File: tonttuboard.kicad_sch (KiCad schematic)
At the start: 45 parts, among them U3 ICM-40609-D, U4 BMP388, U5 W25Q256JVFIQT, U6 MMC5983MA, U9 Teensy 4.0

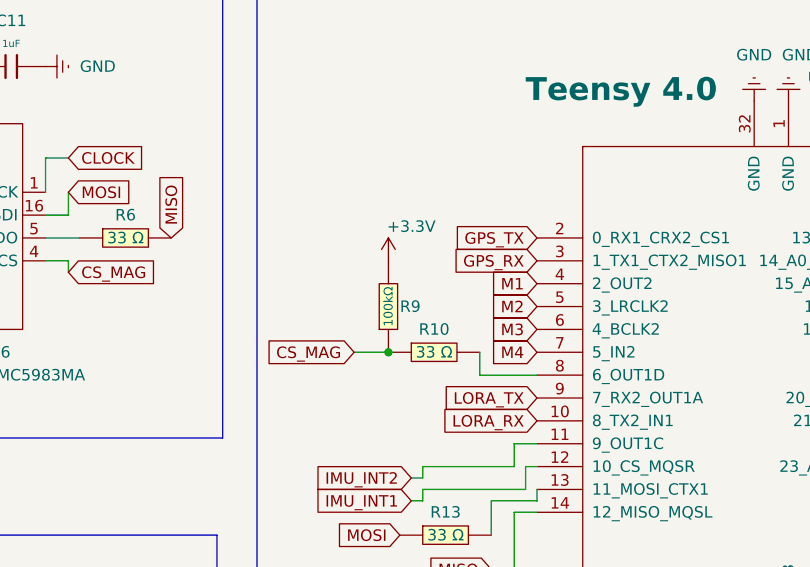
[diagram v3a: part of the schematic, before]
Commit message: Changed the CS Magnetometer 100 kohm pull-up to 4.7 kohm pulldown
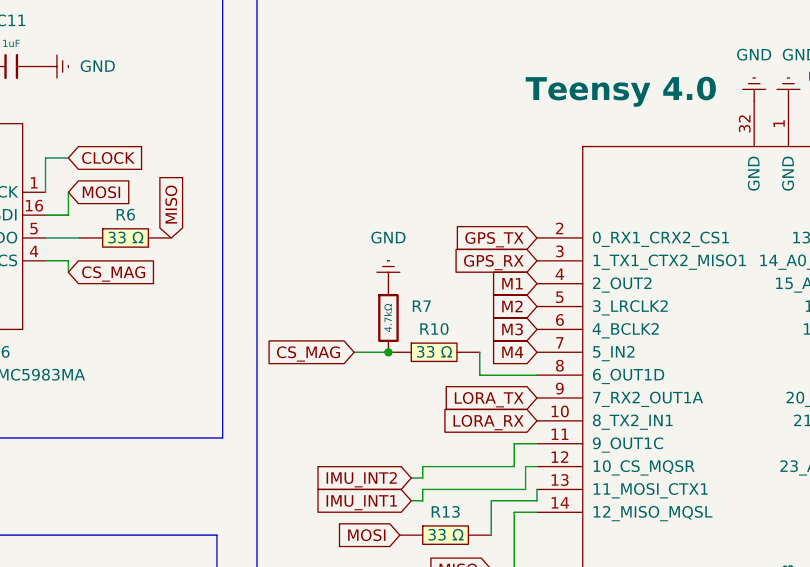
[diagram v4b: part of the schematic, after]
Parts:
- removed R9: 0603WAF1003T5E, EasyEDA:R0603, symbol EasyEDA:0603WAF1003T5E
- added R7: 4.7kΩ, PCM_JLCPCB:R_0603, symbol PCM_JLCPCB-Resistors:0603,4.7kΩ
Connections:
- net CS_MAG: now also R7.2
- net GND: now also R7.1
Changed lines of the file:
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@@
 	)
 	(junction
+		(at 179.07 66.04)
+		(diameter 0)
+		(color 0 0 0 0)
+	)
+	(junction
 		(at 58.42 97.79)
 		(diameter 0)
@@
 	)
 	(junction
-		(at 179.07 66.04)
-		(diameter 0)
-		(color 0 0 0 0)
-	)
-	(junction
 		(at 127 95.25)
 		(diameter 0)
@@
 	)
 	(symbol
-		(lib_id "power:+3.3V")
-		(at 179.07 55.88 0)
-		(unit 1)
-		(exclude_from_sim no)
-		(in_bom yes)
-		(on_board yes)
-		(dnp no)
-		(property "Reference" "#PWR042"
-			(at 179.07 59.69 0)
-			(effects
-				(font
-					(size 1.27 1.27)
-				)
-				(hide yes)
-			)
-		)
-		(property "Value" "+3.3V"
-			(at 181.61 52.07 0)
-			(effects
-				(font
-					(size 1.27 1.27)
-				)
-			)
-		)
-		(property "Footprint" ""
-			(at 179.07 55.88 0)
-			(effects
-				(font
-					(size 1.27 1.27)
-				)
-				(hide yes)
-			)
-		)
-		(property "Datasheet" ""
-			(at 179.07 55.88 0)
-			(effects
-				(font
-					(size 1.27 1.27)
-				)
-				(hide yes)
-			)
-		)
-		(property "Description" "Power symbol creates a global label with name \"+3.3V\""
-			(at 179.07 55.88 0)
-			(effects
-				(font
-					(size 1.27 1.27)
-				)
-				(hide yes)
-			)
-		)
-		(pin "1"
-		)
-		(instances
-			(project "tonttulauta v.0"
-				(path "/b9cca3cd-cb2d-42d4-a628-737eddf4a5c6"
-					(reference "#PWR042")
-					(unit 1)
-				)
-			)
-		)
-	)
-	(symbol
 		(lib_id "EasyEDA:BMP388")
 		(at 64.77 45.72 0)
@@
 	)
 	(symbol
+		(lib_id "PCM_JLCPCB-Resistors:0603,4.7kΩ")
+		(at 179.07 62.23 0)
+		(unit 1)
+		(exclude_from_sim no)
+		(in_bom yes)
+		(on_board yes)
+		(dnp no)
+		(property "Reference" "R7"
+			(at 181.61 60.96 0)
+			(effects
+				(font
+					(size 1.27 1.27)
+				)
+				(justify left)
+			)
+		)
+		(property "Value" "4.7kΩ"
+			(at 179.07 62.23 90)
+			(do_not_autoplace yes)
+			(effects
+				(font
+					(size 0.8 0.8)
+				)
+			)
+		)
+		(property "Footprint" "PCM_JLCPCB:R_0603"
+			(at 177.292 62.23 90)
+			(effects
+				(font
+					(size 1.27 1.27)
+				)
+				(hide yes)
+			)
+		)
+		(property "Datasheet" "https://www.lcsc.com/datasheet/lcsc_datasheet_2206010116_UNI-ROYAL-Uniroyal-Elec-0603WAF4701T5E_C23162.pdf"
+			(at 179.07 62.23 0)
+			(effects
+				(font
+					(size 1.27 1.27)
+				)
+				(hide yes)
+			)
+		)
+		(property "Description" "100mW Thick Film Resistors 75V ±100ppm/°C ±1% 4.7kΩ 0603 Chip Resistor - Surface Mount ROHS"
+			(at 179.07 62.23 0)
+			(effects
+				(font
+					(size 1.27 1.27)
+				)
+				(hide yes)
+			)
+		)
+		(property "LCSC" "C23162"
+			(at 179.07 62.23 0)
+			(effects
+				(font
+					(size 1.27 1.27)
+				)
+				(hide yes)
+			)
+		)
+		(property "Stock" "11302490"
+			(at 179.07 62.23 0)
+			(effects
+				(font
+					(size 1.27 1.27)
+				)
+				(hide yes)
+			)
+		)
+		(property "Price" "0.004USD"
+			(at 179.07 62.23 0)
+			(effects
+				(font
+					(size 1.27 1.27)
+				)
+				(hide yes)
+			)
+		)
+		(property "Process" "SMT"
+			(at 179.07 62.23 0)
+			(effects
+				(font
+					(size 1.27 1.27)
+				)
+				(hide yes)
+			)
+		)
+		(property "Minimum Qty" "20"
+			(at 179.07 62.23 0)
+			(effects
+				(font
+					(size 1.27 1.27)
+				)
+				(hide yes)
+			)
+		)
+		(property "Attrition Qty" "10"
+			(at 179.07 62.23 0)
+			(effects
+				(font
+					(size 1.27 1.27)
+				)
+				(hide yes)
+			)
+		)
+		(property "Class" "Basic Component"
+			(at 179.07 62.23 0)
+			(effects
+				(font
+					(size 1.27 1.27)
+				)
+				(hide yes)
+			)
+		)
+		(property "Category" "Resistors,Chip Resistor - Surface Mount"
+			(at 179.07 62.23 0)
+			(effects
+				(font
+					(size 1.27 1.27)
+				)
+				(hide yes)
+			)
+		)
+		(property "Manufacturer" "UNI-ROYAL(Uniroyal Elec)"
+			(at 179.07 62.23 0)
+			(effects
+				(font
+					(size 1.27 1.27)
+				)
+				(hide yes)
+			)
+		)
+		(property "Part" "0603WAF4701T5E"
+			(at 179.07 62.23 0)
+			(effects
+				(font
+					(size 1.27 1.27)
+				)
+				(hide yes)
+			)
+		)
+		(property "Resistance" "4.7kΩ"
+			(at 179.07 62.23 0)
+			(effects
+				(font
+					(size 1.27 1.27)
+				)
+				(hide yes)
+			)
+		)
+		(property "Power(Watts)" "100mW"
+			(at 179.07 62.23 0)
+			(effects
+				(font
+					(size 1.27 1.27)
+				)
+				(hide yes)
+			)
+		)
+		(property "Type" "Thick Film Resistors"
+			(at 179.07 62.23 0)
+			(effects
+				(font
+					(size 1.27 1.27)
+				)
+				(hide yes)
+			)
+		)
+		(property "Overload Voltage (Max)" "75V"
+			(at 179.07 62.23 0)
+			(effects
+				(font
+					(size 1.27 1.27)
+				)
+				(hide yes)
+			)
+		)
+		(property "Operating Temperature Range" "-55°C~+155°C"
+			(at 179.07 62.23 0)
+			(effects
+				(font
+					(size 1.27 1.27)
+				)
+				(hide yes)
+			)
+		)
+		(property "Tolerance" "±1%"
+			(at 179.07 62.23 0)
+			(effects
+				(font
+					(size 1.27 1.27)
+				)
+				(hide yes)
+			)
+		)
+		(property "Temperature Coefficient" "±100ppm/°C"
+			(at 179.07 62.23 0)
+			(effects
+				(font
+					(size 1.27 1.27)
+				)
+				(hide yes)
+			)
+		)
+		(pin "2"
+		)
+		(pin "1"
+		)
+		(instances
+			(project ""
+				(path "/b9cca3cd-cb2d-42d4-a628-737eddf4a5c6"
+					(reference "R7")
+					(unit 1)
+				)
+			)
+		)
+	)
+	(symbol
 		(lib_id "PCM_JLCPCB-Capacitors:0603,100nF")
 		(at 64.77 97.79 90)
@@
 	)
 	(symbol
+		(lib_id "power:Earth")
+		(at 179.07 58.42 180)
+		(unit 1)
+		(exclude_from_sim no)
+		(in_bom yes)
+		(on_board yes)
+		(dnp no)
+		(fields_autoplaced yes)
+		(property "Reference" "#PWR060"
+			(at 179.07 52.07 0)
+			(effects
+				(font
+					(size 1.27 1.27)
+				)
+				(hide yes)
+			)
+		)
+		(property "Value" "GND"
+			(at 179.07 53.34 0)
+			(effects
+				(font
+					(size 1.27 1.27)
+				)
+			)
+		)
+		(property "Footprint" ""
+			(at 179.07 58.42 0)
+			(effects
+				(font
+					(size 1.27 1.27)
+				)
+				(hide yes)
+			)
+		)
+		(property "Datasheet" "~"
+			(at 179.07 58.42 0)
+			(effects
+				(font
+					(size 1.27 1.27)
+				)
+				(hide yes)
+			)
+		)
+		(property "Description" "Power symbol creates a global label with name \"Earth\""
+			(at 179.07 58.42 0)
+			(effects
+				(font
+					(size 1.27 1.27)
+				)
+				(hide yes)
+			)
+		)
+		(pin "1"
+		)
+		(instances
+			(project "tonttuboard"
+				(path "/b9cca3cd-cb2d-42d4-a628-737eddf4a5c6"
+					(reference "#PWR060")
+					(unit 1)
+				)
+			)
+		)
+	)
+	(symbol
 		(lib_id "power:+3.3V")
 		(at 113.03 118.11 90)
@@
 					(unit 1)
 				)
-			)
-		)
-	)
-	(symbol
-		(lib_id "EasyEDA:0603WAF1003T5E")
-		(at 179.07 60.96 90)
-		(unit 1)
-		(exclude_from_sim no)
-		(in_bom yes)
-		(on_board yes)
-		(dnp no)
-		(property "Reference" "R9"
-			(at 180.34 60.96 90)
-			(effects
-				(font
-					(size 1.27 1.27)
-				)
-				(justify right)
-			)
-		)
-		(property "Value" "0603WAF1003T5E"
-			(at 181.61 62.2299 90)
-			(effects
-				(font
-					(size 1.27 1.27)
-				)
-				(justify right)
-				(hide yes)
-			)
-		)
-		(property "Footprint" "EasyEDA:R0603"
-			(at 186.69 60.96 0)
-			(effects
-				(font
-					(size 1.27 1.27)
-				)
-				(hide yes)
-			)
-		)
-		(property "Datasheet" "https://lcsc.com/product-detail/Chip-Resistor-Surface-Mount-UniOhm_100KR-1003-1_C25803.html"
-			(at 189.23 60.96 0)
-			(effects
-				(font
-					(size 1.27 1.27)
-				)
-				(hide yes)
-			)
-		)
-		(property "Description" "100kΩ"
-			(at 179.07 60.96 0)
-			(do_not_autoplace yes)
-			(effects
-				(font
-					(size 1 1)
-				)
-			)
-		)
-		(property "LCSC Part" "C25803"
-			(at 191.77 60.96 0)
-			(effects
-				(font
-					(size 1.27 1.27)
-				)
-				(hide yes)
-			)
-		)
-		(pin "1"
-		)
-		(pin "2"
-		)
-		(instances
-			(project "tonttulauta v.0"
-				(path "/b9cca3cd-cb2d-42d4-a628-737eddf4a5c6"
-					(reference "R9")
-					(unit 1)
-				)

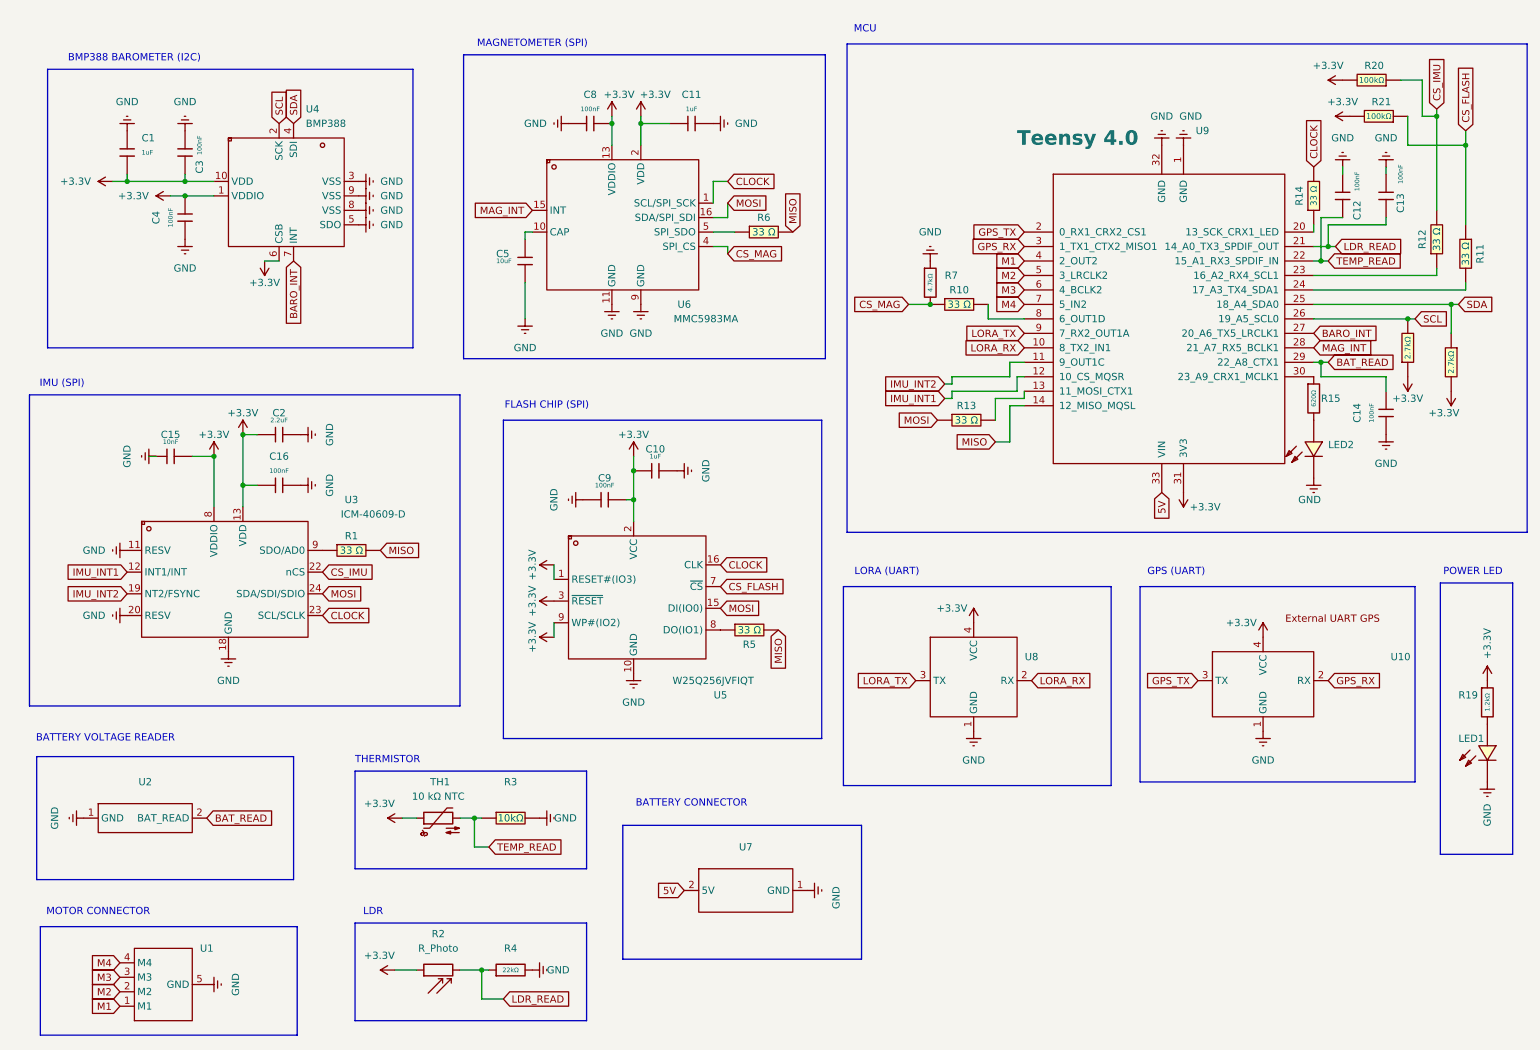
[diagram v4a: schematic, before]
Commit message: Removed magnetometer and changed component placement
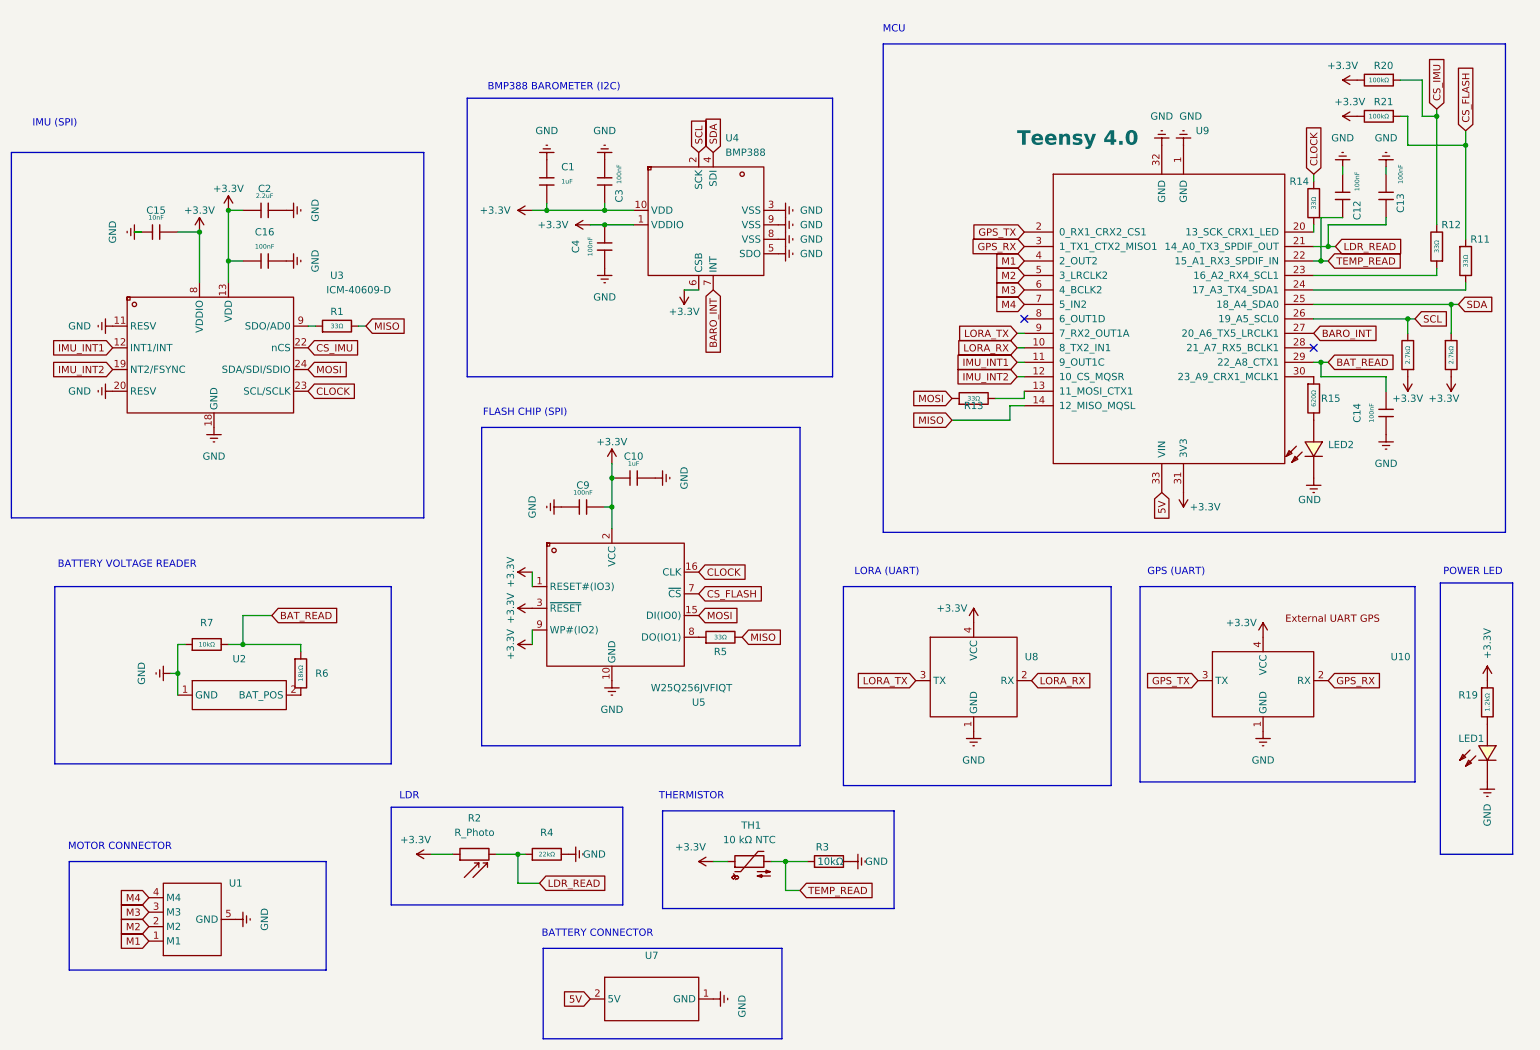
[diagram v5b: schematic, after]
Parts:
- removed C11: 1uF, PCM_JLCPCB:C_0603, symbol PCM_JLCPCB-Capacitors:0603,1uF
- removed C5: 10uF, PCM_JLCPCB:C_0603, symbol PCM_JLCPCB-Capacitors:0603,10uF
- removed C8: 100nF, PCM_JLCPCB:C_0603, symbol PCM_JLCPCB-Capacitors:0603,100nF
- removed R10, R6: RC0603FR-0733RL, EasyEDA:R0603, symbol EasyEDA:RC0603FR-0733RL
- removed R7: 4.7kΩ, PCM_JLCPCB:R_0603, symbol PCM_JLCPCB-Resistors:0603,4.7kΩ
- removed U6: MMC5983MA, EasyEDA:LGA-16_L3.0-W3.0-P0.50-BL_SQ, symbol EasyEDA:MMC5983MA
- added R6: 18kΩ, PCM_JLCPCB:R_0603, symbol PCM_JLCPCB-Resistors:0603,18kΩ
- added R7: 10kΩ, PCM_JLCPCB:R_0603, symbol PCM_JLCPCB-Resistors:0603,10kΩ
- R1, R11, R12, R13, R14, R5: value RC0603FR-0733RL -> 33Ω; footprint EasyEDA:R0603 -> PCM_JLCPCB:R_0603; symbol EasyEDA:RC0603FR-0733RL -> PCM_JLCPCB-Resistors:0603,33Ω; LCSC (none) -> C23140; Tolerance (none) -> ±1%
- R16, R17: value 0603WAF2701T5E -> 2.7kΩ; footprint EasyEDA:R0603 -> PCM_JLCPCB:R_0603; symbol EasyEDA:0603WAF2701T5E -> PCM_JLCPCB-Resistors:0603,2.7kΩ; LCSC (none) -> C13167
- R20, R21: value 0603WAF1003T5E -> 100kΩ; footprint EasyEDA:R0603 -> PCM_JLCPCB:R_0603; symbol EasyEDA:0603WAF1003T5E -> PCM_JLCPCB-Resistors:0603,100kΩ; Attrition Qty (none) -> 10; Category (none) -> Resistors,Chip Resistor - Surface Mount; Class (none) -> Basic Component; LCSC (none) -> C25803; Manufacturer (none) -> UNI-ROYAL(Uniroyal Elec); Minimum Qty (none) -> 20; Operating Temperature Range (none) -> -55°C~+155°C; Overload Voltage (Max) (none) -> 75V; Part (none) -> 0603WAF1003T5E; Power(Watts) (none) -> 100mW; Price (none) -> 0.004USD; Process (none) -> SMT; Resistance (none) -> 100kΩ; Stock (none) -> 7820113; Temperature Coefficient (none) -> ±100ppm/°C; Tolerance (none) -> ±1%; Type (none) -> Thick Film Resistors
- R3: footprint EasyEDA:R0603 -> PCM_JLCPCB:R_0603; symbol EasyEDA:0603WAF1002T5E -> PCM_JLCPCB-Resistors:0603,10kΩ; Attrition Qty (none) -> 10; Category (none) -> Resistors,Chip Resistor - Surface Mount; Class (none) -> Basic Component; LCSC (none) -> C25804; Manufacturer (none) -> UNI-ROYAL(Uniroyal Elec); Minimum Qty (none) -> 20; Operating Temperature Range (none) -> -55°C~+155°C; Overload Voltage (Max) (none) -> 75V; Part (none) -> 0603WAF1002T5E; Power(Watts) (none) -> 100mW; Price (none) -> 0.004USD; Process (none) -> SMT; Resistance (none) -> 10kΩ; Stock (none) -> 51181774; Temperature Coefficient (none) -> ±100ppm/°C; Tolerance (none) -> ±1%; Type (none) -> Thick Film Resistors
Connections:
- net BAT_READ: now also R6.1, R7.2; no longer U2.2 (BAT_READ)
- net GND: now also R7.1
- net IMU_INT1: now also U9.11 (9_OUT1C); no longer U9.12 (10_CS_MQSR)
- net IMU_INT2: now also U9.12 (10_CS_MQSR); no longer U9.11 (9_OUT1C)
- net MAG_INT: no longer names the net of U9.28 (21_A7_RX5_BCLK1)
- new net: R6.2, U2.2 (BAT_POS)
- no-connect marks 0 -> 2
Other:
- note removed: "MAGNETOMETER (SPI)"
- moved on the sheet: C1, C10, C15, C16, C2, C3, C4, C9, R2, R4, TH1, U1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
